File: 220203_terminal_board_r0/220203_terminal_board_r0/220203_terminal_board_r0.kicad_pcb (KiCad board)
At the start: 2 copper layers, 161.4 x 108 mm, 37 parts

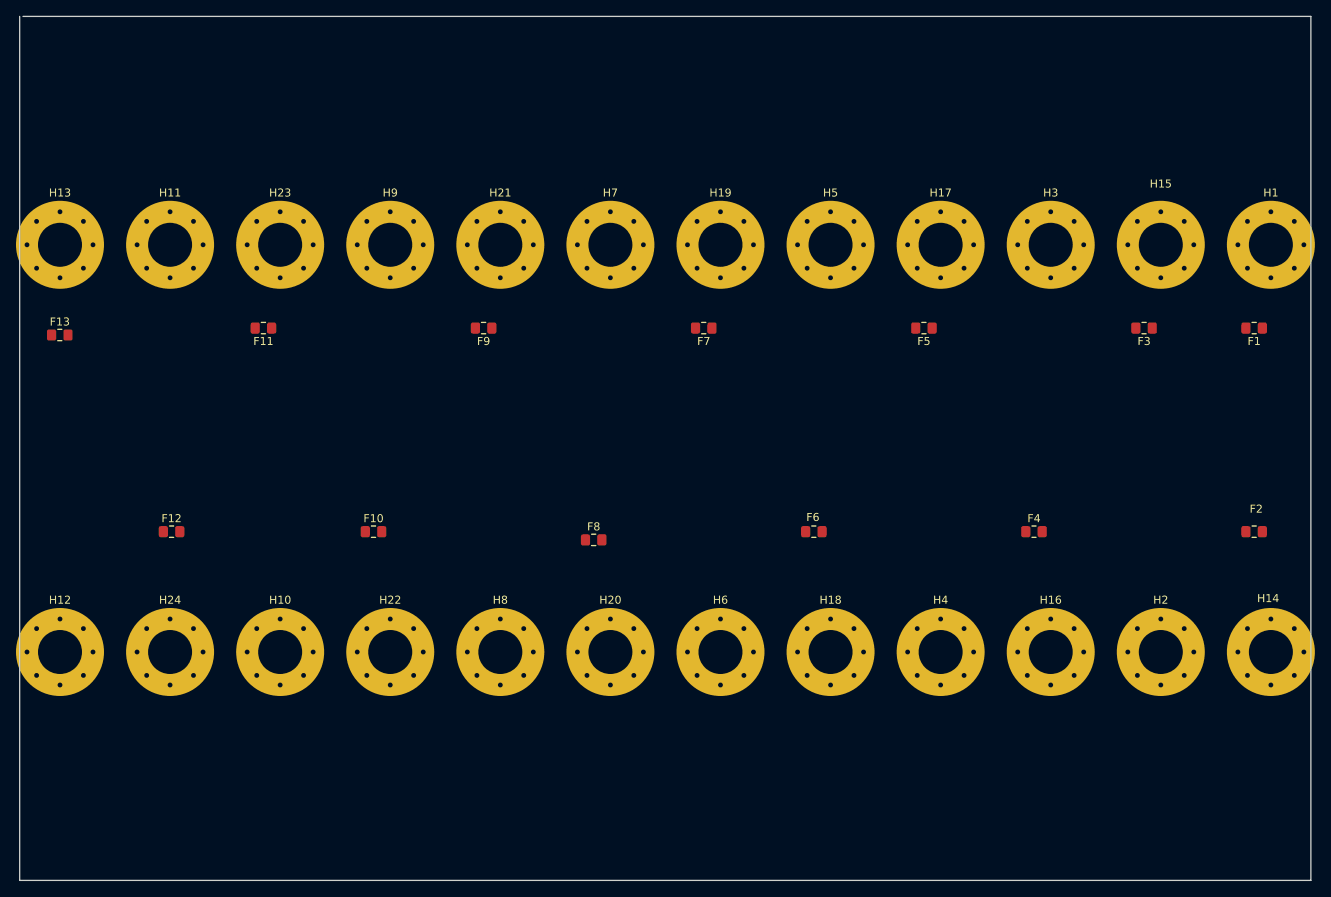
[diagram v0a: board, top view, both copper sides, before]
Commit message: minor BOM changes
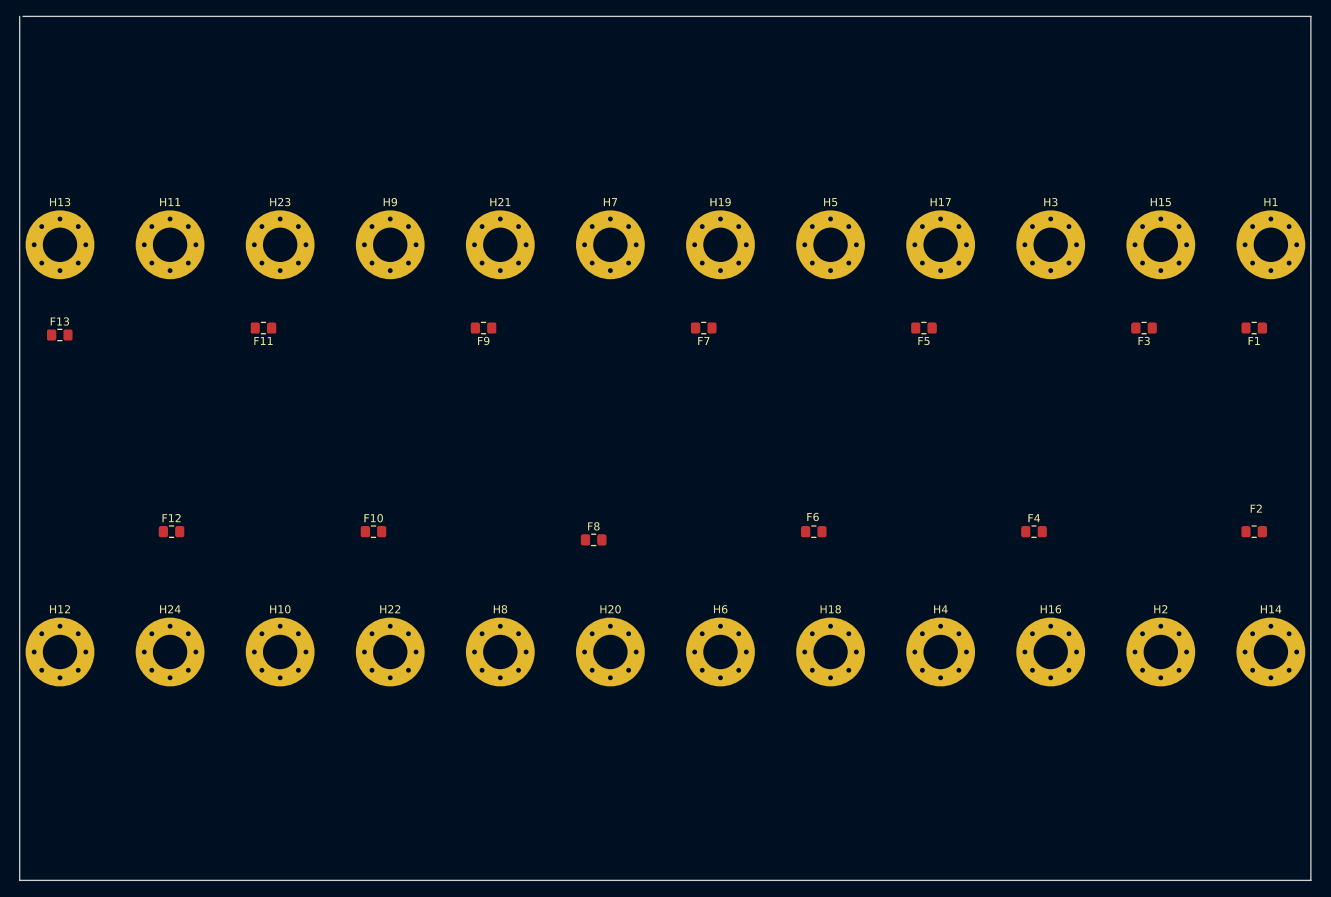
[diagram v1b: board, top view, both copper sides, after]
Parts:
- H1, H10, H11, H12, H13, H14, H15, H16, H17, H18, H19, H2, H20, H21, H22, H23, H24, H3, H4, H5, H6, H7, H8, H9: footprint MountingHole:MountingHole_5.5mm_Pad_Via -> MountingHole:MountingHole_4.3mm_M4_Pad_Via
